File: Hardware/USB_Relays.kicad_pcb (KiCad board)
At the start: 2 copper layers, 11 parts, among them J1 2411_06, U1 FT230XS

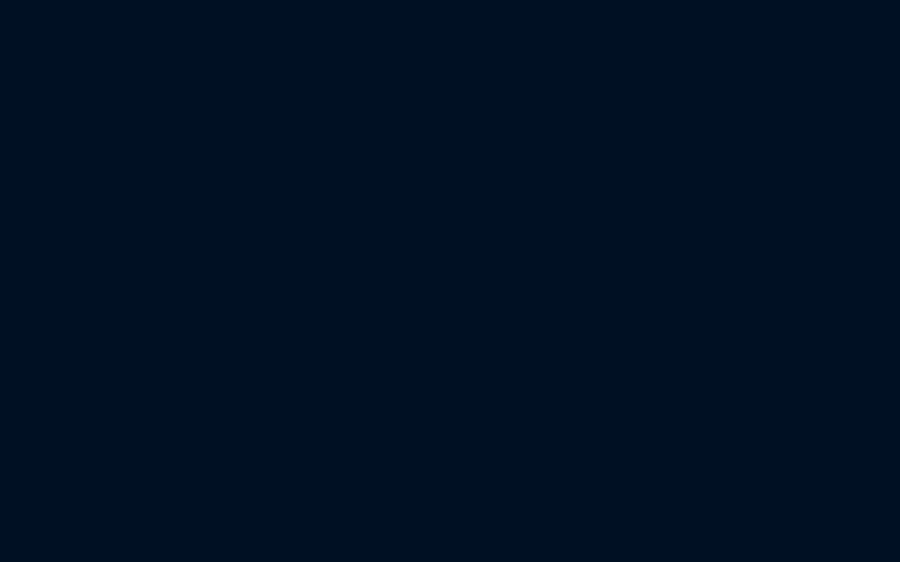
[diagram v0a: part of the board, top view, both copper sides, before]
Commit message: [Hardware] Added HRS1H-S DC5V relay symbol, footprint and 3D model.
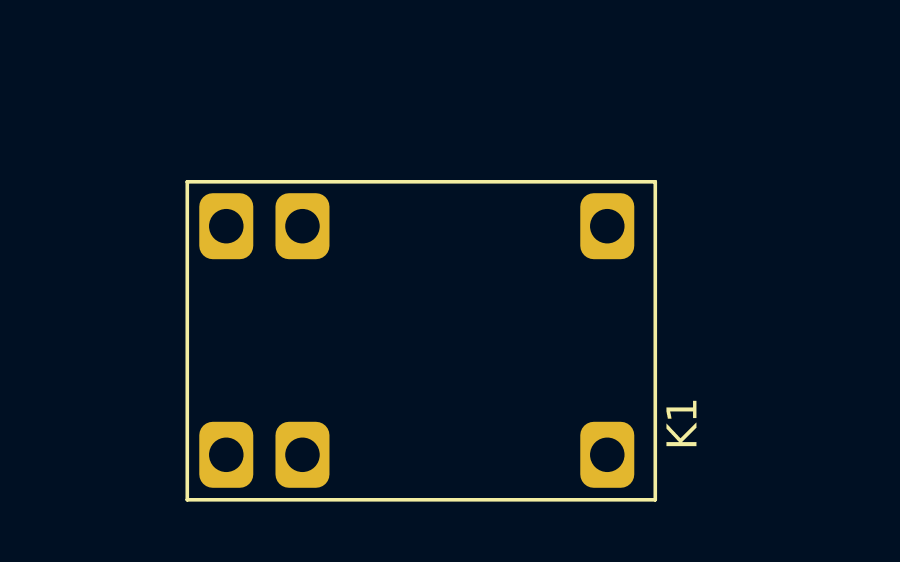
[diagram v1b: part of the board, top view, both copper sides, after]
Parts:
- added K1: HRS1H-S_DC5V, HRS1H-S:HRS1H-S, F.Cu at (152.4, 61.7)
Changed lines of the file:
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@@
     (tracks 0)
     (zones 0)
-    (modules 11)
-    (nets 16)
+    (modules 12)
+    (nets 21)
   )
   (page A4)
@@
   (net 14 "Net-(U1-Pad2)")
   (net 15 FTDI_TX)
+  (net 16 "Net-(K1-Pad3)")
+  (net 17 "Net-(K1-Pad4)")
+  (net 18 "Net-(K1-Pad2)")
+  (net 19 "Net-(K1-Pad6)")
+  (net 20 "Net-(K1-Pad1)")
   (net_class Default "This is the default net class."
     (clearance 0.2)
@@
     (add_net FTDI_TX)
     (add_net GND)
+    (add_net "Net-(K1-Pad1)")
+    (add_net "Net-(K1-Pad2)")
+    (add_net "Net-(K1-Pad3)")
+    (add_net "Net-(K1-Pad4)")
+    (add_net "Net-(K1-Pad6)")
     (add_net "Net-(U1-Pad14)")
     (add_net "Net-(U1-Pad15)")
@@
     (add_net "Net-(U1-Pad7)")
   )
+  (module HRS1H-S:HRS1H-S (layer F.Cu)
+    (at 152.4 61.722)
+    (fp_text reference K1 (at 8.86 2.77 270) (layer F.SilkS)
+      (effects (font (size 1 1) (thickness 0.15)))
+    )
+    (fp_text value HRS1H-S_DC5V (at -0.03 0.23) (layer F.Fab)
+      (effects (font (size 1 1) (thickness 0.15)))
+    )
+    (fp_line (start -7.65 5.31) (end -7.65 -5.29) (layer F.SilkS) (width 0.12))
+    (fp_line (start -7.65 -5.29) (end 7.95 -5.29) (layer F.SilkS) (width 0.12))
+    (fp_line (start 7.95 -5.29) (end 7.95 5.31) (layer F.SilkS) (width 0.12))
+    (fp_line (start 7.95 5.31) (end -7.65 5.31) (layer F.SilkS) (width 0.12))
+    (fp_line (start -7.65 5.31) (end -7.65 -5.29) (layer F.Fab) (width 0.12))
+    (fp_line (start -7.65 -5.29) (end 7.95 -5.29) (layer F.Fab) (width 0.12))
+    (fp_line (start 7.95 -5.29) (end 7.95 5.31) (layer F.Fab) (width 0.12))
+    (fp_line (start 7.95 5.31) (end -7.65 5.31) (layer F.Fab) (width 0.12))
+    (pad 3 thru_hole roundrect (at 6.35 3.81) (size 1.8 2.2) (drill 1.15) (layers *.Cu *.Mask) (roundrect_rratio 0.25)
+      (net 16 "Net-(K1-Pad3)"))
+    (pad 4 thru_hole roundrect (at 6.35 -3.81) (size 1.8 2.2) (drill 1.15) (layers *.Cu *.Mask) (roundrect_rratio 0.25)
+      (net 17 "Net-(K1-Pad4)"))
+    (pad 2 thru_hole roundrect (at -3.81 -3.81) (size 1.8 2.2) (drill 1.15) (layers *.Cu *.Mask) (roundrect_rratio 0.25)
+      (net 18 "Net-(K1-Pad2)"))
+    (pad 6 thru_hole roundrect (at -6.35 -3.81) (size 1.8 2.2) (drill 1.15) (layers *.Cu *.Mask) (roundrect_rratio 0.25)
+      (net 19 "Net-(K1-Pad6)"))
+    (pad 1 thru_hole roundrect (at -6.35 3.81) (size 1.8 2.2) (drill 1.15) (layers *.Cu *.Mask) (roundrect_rratio 0.25)
+      (net 20 "Net-(K1-Pad1)"))
+    (pad 2 thru_hole roundrect (at -3.81 3.81) (size 1.8 2.2) (drill 1.15) (layers *.Cu *.Mask) (roundrect_rratio 0.25)
+      (net 18 "Net-(K1-Pad2)"))
+    (model ${KIPRJMOD}/HRS1H-S.pretty/HRS1H-S.step
+      (offset (xyz 7.65 5.25 0))
+      (scale (xyz 1 1 1))
+      (rotate (xyz 0 0 0))
+    )
+  )
   (module Package_SO:SSOP-16_3.9x4.9mm_P0.635mm (layer F.Cu)

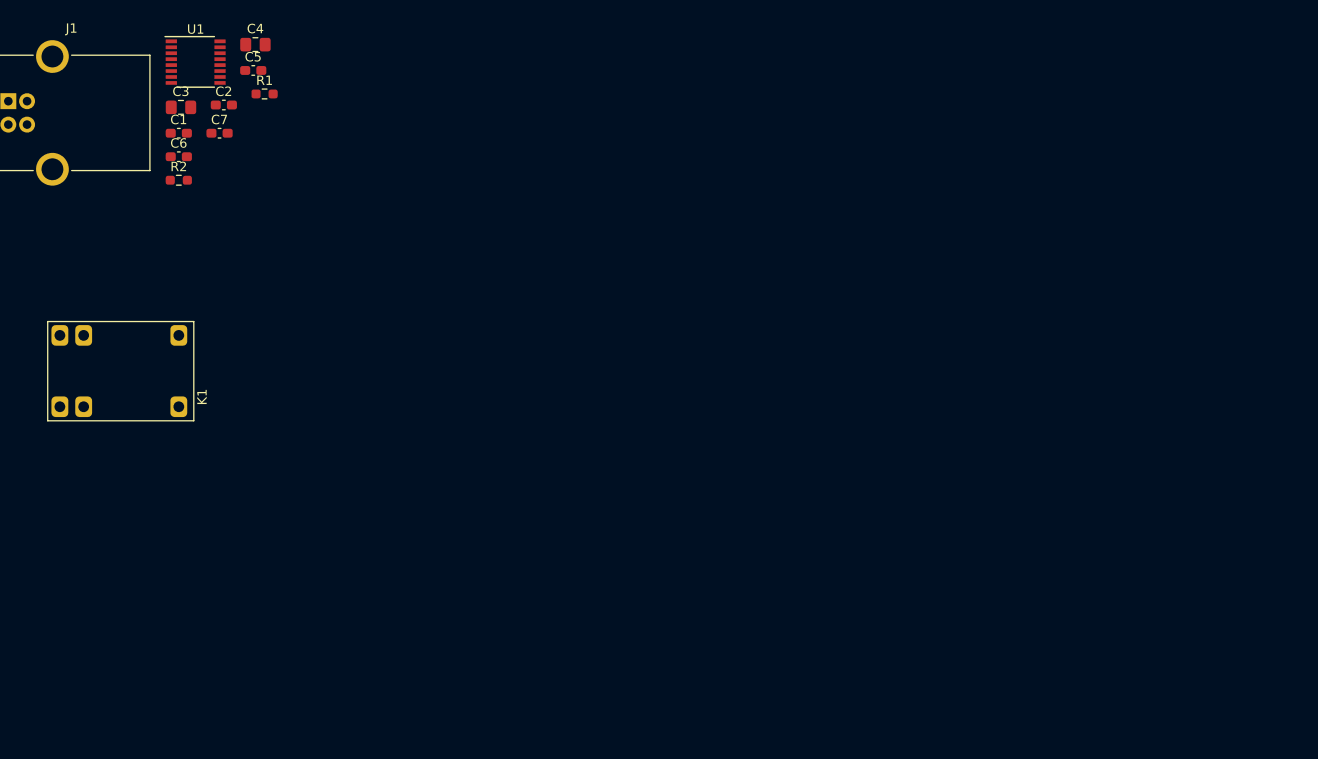
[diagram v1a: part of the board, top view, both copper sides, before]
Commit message: [Hardware] Added relays schematic sheet.
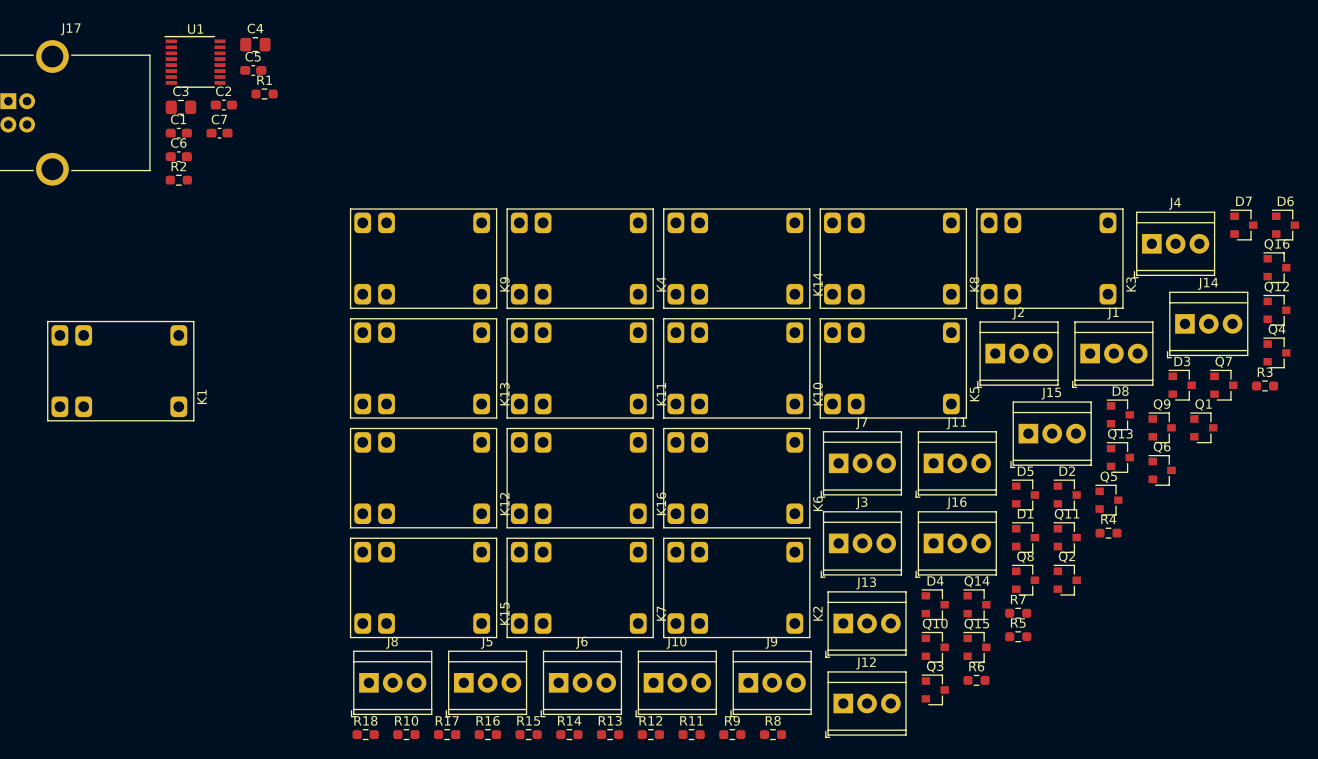
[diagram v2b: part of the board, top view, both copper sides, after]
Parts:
- added D1: BAT54C, Package_TO_SOT_SMD:SOT-23, F.Cu at (249.2, 79.5)
- added D2: BAT54C, Package_TO_SOT_SMD:SOT-23, F.Cu at (253.6, 75.0)
- added D3: BAT54C, Package_TO_SOT_SMD:SOT-23, F.Cu at (265.9, 63.2)
- added D4: BAT54C, Package_TO_SOT_SMD:SOT-23, F.Cu at (239.5, 86.7)
- added D5: BAT54C, Package_TO_SOT_SMD:SOT-23, F.Cu at (249.2, 75.0)
- added D6: BAT54C, Package_TO_SOT_SMD:SOT-23, F.Cu at (276.9, 46.1)
- added D7: BAT54C, Package_TO_SOT_SMD:SOT-23, F.Cu at (272.5, 46.1)
- added D8: BAT54C, Package_TO_SOT_SMD:SOT-23, F.Cu at (259.3, 66.4)
- added J1: 282834-3, TerminalBlock_TE-Connectivity:TerminalBlock_TE_282834-3_1x03_P2.54mm_Horizontal, F.Cu at (256.1, 59.9)
- added J10: 282834-3, TerminalBlock_TE-Connectivity:TerminalBlock_TE_282834-3_1x03_P2.54mm_Horizontal, F.Cu at (209.4, 95.0)
- added J11: 282834-3, TerminalBlock_TE-Connectivity:TerminalBlock_TE_282834-3_1x03_P2.54mm_Horizontal, F.Cu at (239.3, 71.6)
- added J12: 282834-3, TerminalBlock_TE-Connectivity:TerminalBlock_TE_282834-3_1x03_P2.54mm_Horizontal, F.Cu at (229.7, 97.2)
- added J13: 282834-3, TerminalBlock_TE-Connectivity:TerminalBlock_TE_282834-3_1x03_P2.54mm_Horizontal, F.Cu at (229.7, 88.7)
- added J14: 282834-3, TerminalBlock_TE-Connectivity:TerminalBlock_TE_282834-3_1x03_P2.54mm_Horizontal, F.Cu at (266.2, 56.7)
- added J15: 282834-3, TerminalBlock_TE-Connectivity:TerminalBlock_TE_282834-3_1x03_P2.54mm_Horizontal, F.Cu at (249.5, 68.4)
- added J16: 282834-3, TerminalBlock_TE-Connectivity:TerminalBlock_TE_282834-3_1x03_P2.54mm_Horizontal, F.Cu at (239.3, 80.1)
- added J2: 282834-3, TerminalBlock_TE-Connectivity:TerminalBlock_TE_282834-3_1x03_P2.54mm_Horizontal, F.Cu at (245.9, 59.9)
- added J3: 282834-3, TerminalBlock_TE-Connectivity:TerminalBlock_TE_282834-3_1x03_P2.54mm_Horizontal, F.Cu at (229.2, 80.1)
- added J4: 282834-3, TerminalBlock_TE-Connectivity:TerminalBlock_TE_282834-3_1x03_P2.54mm_Horizontal, F.Cu at (262.7, 48.1)
- added J5: 282834-3, TerminalBlock_TE-Connectivity:TerminalBlock_TE_282834-3_1x03_P2.54mm_Horizontal, F.Cu at (189.2, 95.0)
- added J6: 282834-3, TerminalBlock_TE-Connectivity:TerminalBlock_TE_282834-3_1x03_P2.54mm_Horizontal, F.Cu at (199.3, 95.0)
- added J7: 282834-3, TerminalBlock_TE-Connectivity:TerminalBlock_TE_282834-3_1x03_P2.54mm_Horizontal, F.Cu at (229.2, 71.6)
- added J8: 282834-3, TerminalBlock_TE-Connectivity:TerminalBlock_TE_282834-3_1x03_P2.54mm_Horizontal, F.Cu at (179.1, 95.0)
- added J9: 282834-3, TerminalBlock_TE-Connectivity:TerminalBlock_TE_282834-3_1x03_P2.54mm_Horizontal, F.Cu at (219.6, 95.0)
- added K10: HRS1H-S_DC5V, HRS1H-S:HRS1H-S, F.Cu at (218.2, 61.4)
- added K11: HRS1H-S_DC5V, HRS1H-S:HRS1H-S, F.Cu at (201.5, 61.4)
- added K12: HRS1H-S_DC5V, HRS1H-S:HRS1H-S, F.Cu at (184.7, 73.1)
- added K13: HRS1H-S_DC5V, HRS1H-S:HRS1H-S, F.Cu at (184.7, 61.4)
- added K14: HRS1H-S_DC5V, HRS1H-S:HRS1H-S, F.Cu at (218.2, 49.7)
- added K15: HRS1H-S_DC5V, HRS1H-S:HRS1H-S, F.Cu at (184.7, 84.9)
- added K16: HRS1H-S_DC5V, HRS1H-S:HRS1H-S, F.Cu at (201.5, 73.1)
- added K2: HRS1H-S_DC5V, HRS1H-S:HRS1H-S, F.Cu at (218.2, 84.9)
- added K3: HRS1H-S_DC5V, HRS1H-S:HRS1H-S, F.Cu at (251.6, 49.7)
- added K4: HRS1H-S_DC5V, HRS1H-S:HRS1H-S, F.Cu at (201.5, 49.7)
- added K5: HRS1H-S_DC5V, HRS1H-S:HRS1H-S, F.Cu at (234.9, 61.4)
- added K6: HRS1H-S_DC5V, HRS1H-S:HRS1H-S, F.Cu at (218.2, 73.1)
- added K7: HRS1H-S_DC5V, HRS1H-S:HRS1H-S, F.Cu at (201.5, 84.9)
- added K8: HRS1H-S_DC5V, HRS1H-S:HRS1H-S, F.Cu at (234.9, 49.7)
- added K9: HRS1H-S_DC5V, HRS1H-S:HRS1H-S, F.Cu at (184.7, 49.7)
- added Q1: BC848, Package_TO_SOT_SMD:SOT-23, F.Cu at (268.2, 67.8)
- added Q10: BC848, Package_TO_SOT_SMD:SOT-23, F.Cu at (239.5, 91.2)
- added Q11: BC848, Package_TO_SOT_SMD:SOT-23, F.Cu at (253.6, 79.5)
- added Q12: BC848, Package_TO_SOT_SMD:SOT-23, F.Cu at (276.0, 55.2)
- added Q13: BC848, Package_TO_SOT_SMD:SOT-23, F.Cu at (259.3, 71.0)
- added Q14: BC848, Package_TO_SOT_SMD:SOT-23, F.Cu at (244.0, 86.7)
- added Q15: BC848, Package_TO_SOT_SMD:SOT-23, F.Cu at (244.0, 91.2)
- added Q16: BC848, Package_TO_SOT_SMD:SOT-23, F.Cu at (276.0, 50.7)
- added Q2: BC848, Package_TO_SOT_SMD:SOT-23, F.Cu at (253.6, 84.1)
- added Q3: BC848, Package_TO_SOT_SMD:SOT-23, F.Cu at (239.5, 95.8)
- added Q4: BC848, Package_TO_SOT_SMD:SOT-23, F.Cu at (276.0, 59.8)
- added Q5: BC848, Package_TO_SOT_SMD:SOT-23, F.Cu at (258.1, 75.5)
- added Q6: BC848, Package_TO_SOT_SMD:SOT-23, F.Cu at (263.8, 72.3)
- added Q7: BC848, Package_TO_SOT_SMD:SOT-23, F.Cu at (270.3, 63.2)
- added Q8: BC848, Package_TO_SOT_SMD:SOT-23, F.Cu at (249.2, 84.1)
- added Q9: BC848, Package_TO_SOT_SMD:SOT-23, F.Cu at (263.8, 67.8)
- added R10: 1K, Resistor_SMD:R_0603_1608Metric_Pad0.98x0.95mm_HandSolder, F.Cu at (183.1, 100.5)
- added R11: 1K, Resistor_SMD:R_0603_1608Metric_Pad0.98x0.95mm_HandSolder, F.Cu at (213.5, 100.5)
- added R12: 1K, Resistor_SMD:R_0603_1608Metric_Pad0.98x0.95mm_HandSolder, F.Cu at (209.2, 100.5)
- added R13: 1K, Resistor_SMD:R_0603_1608Metric_Pad0.98x0.95mm_HandSolder, F.Cu at (204.8, 100.5)
- added R14: 1K, Resistor_SMD:R_0603_1608Metric_Pad0.98x0.95mm_HandSolder, F.Cu at (200.5, 100.5)
- added R15: 1K, Resistor_SMD:R_0603_1608Metric_Pad0.98x0.95mm_HandSolder, F.Cu at (196.1, 100.5)
- added R16: 1K, Resistor_SMD:R_0603_1608Metric_Pad0.98x0.95mm_HandSolder, F.Cu at (191.8, 100.5)
- added R17: 1K, Resistor_SMD:R_0603_1608Metric_Pad0.98x0.95mm_HandSolder, F.Cu at (187.4, 100.5)
- added R18: 1K, Resistor_SMD:R_0603_1608Metric_Pad0.98x0.95mm_HandSolder, F.Cu at (178.7, 100.5)
- added R3: 1K, Resistor_SMD:R_0603_1608Metric_Pad0.98x0.95mm_HandSolder, F.Cu at (274.7, 63.3)
- added R4: 1K, Resistor_SMD:R_0603_1608Metric_Pad0.98x0.95mm_HandSolder, F.Cu at (258.0, 79.0)
- added R5: 1K, Resistor_SMD:R_0603_1608Metric_Pad0.98x0.95mm_HandSolder, F.Cu at (248.4, 90.1)
- added R6: 1K, Resistor_SMD:R_0603_1608Metric_Pad0.98x0.95mm_HandSolder, F.Cu at (243.9, 94.8)
- added R7: 1K, Resistor_SMD:R_0603_1608Metric_Pad0.98x0.95mm_HandSolder, F.Cu at (248.4, 87.6)
- added R8: 1K, Resistor_SMD:R_0603_1608Metric_Pad0.98x0.95mm_HandSolder, F.Cu at (222.2, 100.5)
- added R9: 1K, Resistor_SMD:R_0603_1608Metric_Pad0.98x0.95mm_HandSolder, F.Cu at (217.9, 100.5)
- renumbered J1 to J17

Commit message: [Hardware] Added terminal 3D models.
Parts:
- J1, J10, J11, J12, J13, J14, J15, J16, J2, J3, J4, J5, J6, J7, J8, J9: footprint TerminalBlock_TE-Connectivity:TerminalBlock_TE_282834-3_1x03_P2.54mm_Horizontal -> 282834-3:TerminalBlock_TE_282834-3_1x03_P2.54mm_Horizontal

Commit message: [Hardware] Positioned components on PCB.
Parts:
- removed C2: 100n, Capacitor_SMD:C_0603_1608Metric_Pad1.08x0.95mm_HandSolder
- removed C3: 4.7u, Capacitor_SMD:C_0805_2012Metric_Pad1.18x1.45mm_HandSolder
- added C10: 100n, Capacitor_SMD:C_0603_1608Metric_Pad1.08x0.95mm_HandSolder, F.Cu at (56.5, 29.8)
- added C8: 4.7u, Capacitor_SMD:C_0805_2012Metric_Pad1.18x1.45mm_HandSolder, F.Cu at (69.2, 58.4)
- added C9: 100n, Capacitor_SMD:C_0603_1608Metric_Pad1.08x0.95mm_HandSolder, F.Cu at (69.2, 61.0)
- added D9: 150060BS55040, LED_SMD:LED_0201_0603Metric_Pad0.64x0.40mm_HandSolder, F.Cu at (61.0, 17.8)
- added J18: DNP, Connector_PinHeader_2.54mm:PinHeader_1x05_P2.54mm_Vertical, F.Cu at (60.3, 42.5)
- added R19: 10K, Resistor_SMD:R_0603_1608Metric_Pad0.98x0.95mm_HandSolder, F.Cu at (55.6, 33.7)
- added R20: 220, Resistor_SMD:R_0603_1608Metric_Pad0.98x0.95mm_HandSolder, F.Cu at (56.5, 37.5)
- added R21: 240, Resistor_SMD:R_1206_3216Metric_Pad1.30x1.75mm_HandSolder, F.Cu at (62.9, 22.2)
- added U2: PIC16F18854-SO, Package_SO:SOIC-28W_7.5x17.9mm_P1.27mm, F.Cu at (60.3, 57.8)
- moved D3 242.9 mm to (23.5, 79.4), turned to 180 degrees
- moved J4 241.6 mm to (21.6, 63.5), turned to 90 degrees
- moved J1 237.2 mm to (21.6, 24.1), turned to 90 degrees
- moved R3 231.4 mm to (46.4, 26.0), turned to 270 degrees
- moved D1 231.4 mm to (23.5, 28.6), turned to 180 degrees
- moved D2 231.1 mm to (23.5, 54.0), turned to 180 degrees
- moved Q4 230.9 mm to (45.1, 61.0), turned to 180 degrees
- moved Q7 228.0 mm to (45.1, 98.4), turned to 180 degrees
- moved Q1 227.7 mm to (45.1, 22.2), turned to 180 degrees
- moved J2 225.4 mm to (21.6, 38.1), turned to 90 degrees
- moved Q6 219.1 mm to (45.1, 85.7), turned to 180 degrees
- moved K3 217.3 mm to (34.3, 47.6)
- moved D4 216.8 mm to (23.5, 104.8), turned to 180 degrees
- moved R4 215.5 mm to (46.4, 38.7), turned to 270 degrees
- moved Q2 214.2 mm to (45.1, 34.9), turned to 180 degrees
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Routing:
- net Net-(D1-Pad1): track 0.00 -> 12.8 mm
- net Net-(D2-Pad2): track 0.00 -> 7.38 mm
- net Net-(D1-Pad2): track 0.00 -> 7.38 mm
- net Net-(D2-Pad1): track 0.00 -> 7.38 mm

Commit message: [Hardware] Renamed components in a more coherent way.
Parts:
- renumbered C8 to C1, C9 to C2, C10 to C3, C1 to C5, C5 to C6, C6 to C7, C7 to C8, J18 to J17, J17 to J18, R3 to R1, R12 to R10, R13 to R11, R14 to R12, R15 to R13, R16 to R14, R17 to R15, R18 to R16, R19 to R17, R21 to R18, R20 to R19, R4 to R2, R1 to R20, R2 to R21, R5 to R3, R6 to R4, R7 to R5, R8 to R6, R9 to R7, R10 to R8, R11 to R9, U2 to U1, U1 to U2
